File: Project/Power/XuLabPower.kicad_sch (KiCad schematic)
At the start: 16 parts, among them Q1 SQJ138ELP, Q2 SQJ138ELP, U1 LM74502

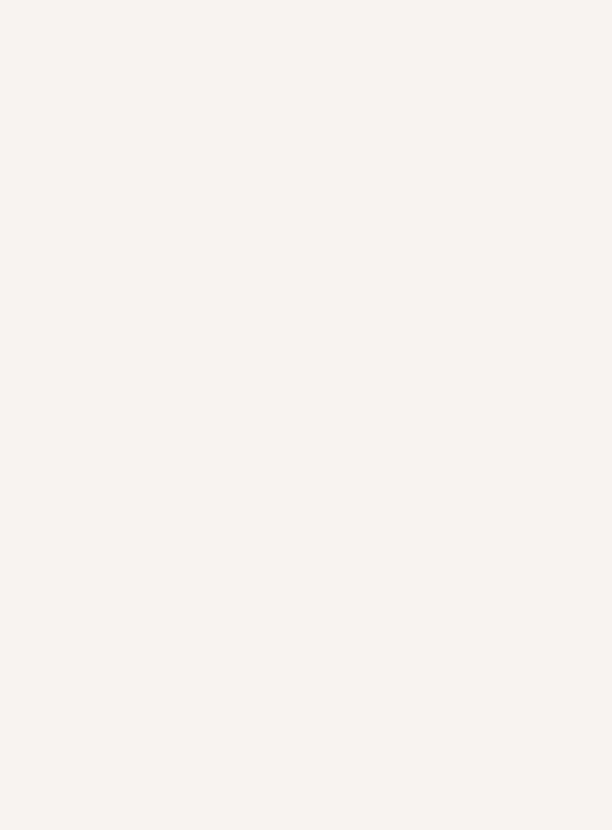
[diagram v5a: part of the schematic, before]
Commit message: Add STM32L422KBTx microcontroller
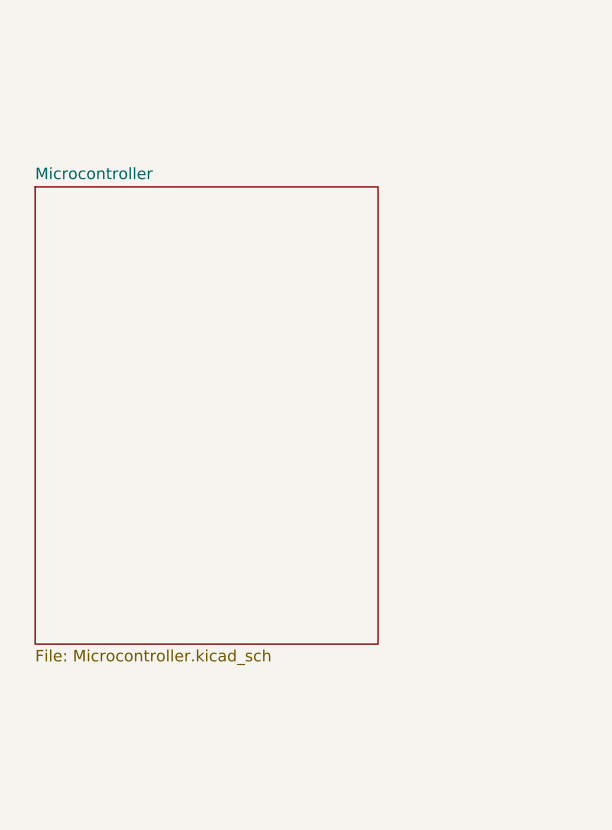
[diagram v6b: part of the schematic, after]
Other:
- added sheet Microcontroller (Microcontroller.kicad_sch)
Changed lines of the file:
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@@
+	)
+	(sheet
+		(at 38.1 88.9)
+		(size 38.1 50.8)
+		(exclude_from_sim no)
+		(in_bom yes)
+		(on_board yes)
+		(dnp no)
+		(fields_autoplaced yes)
+		(stroke
+			(width 0.1524)
+			(type solid)
+		)
+		(fill
+			(color 0 0 0 0.0000)
+		)
+		(property "Sheetname" "Microcontroller"
+			(at 38.1 88.1884 0)
+			(effects
+				(font
+					(size 1.27 1.27)
+				)
+				(justify left bottom)
+			)
+		)
+		(property "Sheetfile" "Microcontroller.kicad_sch"
+			(at 38.1 140.2846 0)
+			(effects
+				(font
+					(size 1.27 1.27)
+				)
+				(justify left top)
+			)
+		)
+		(instances
+			(project "XuLabPower"
+				(path "/71bb14ae-b730-4d22-a41d-cf68989dae2d"
+					(page "3")
+				)
+			)
+		)
 	)
 	(sheet
@@
 			(project "XuLabPower"
 				(path "/71bb14ae-b730-4d22-a41d-cf68989dae2d"
-					(page "3")
+					(page "4")
 				)
 			)

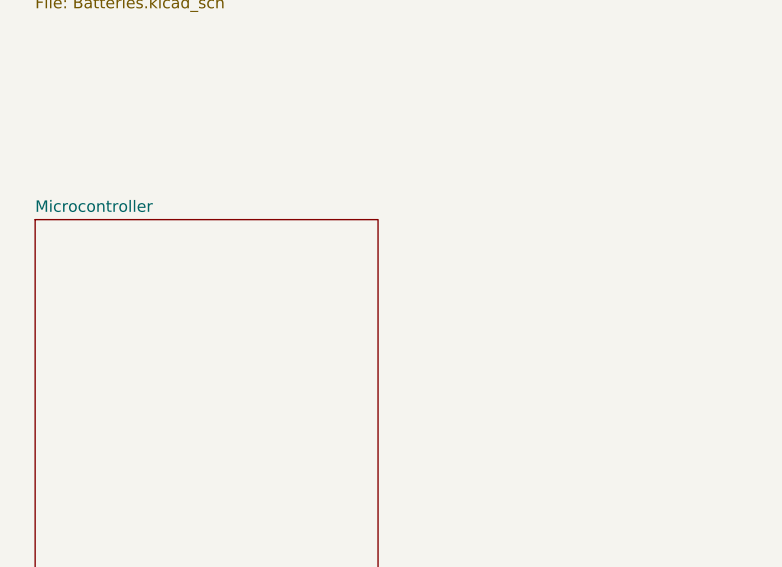
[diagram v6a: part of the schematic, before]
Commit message: Connect microcontroller to main enable switch
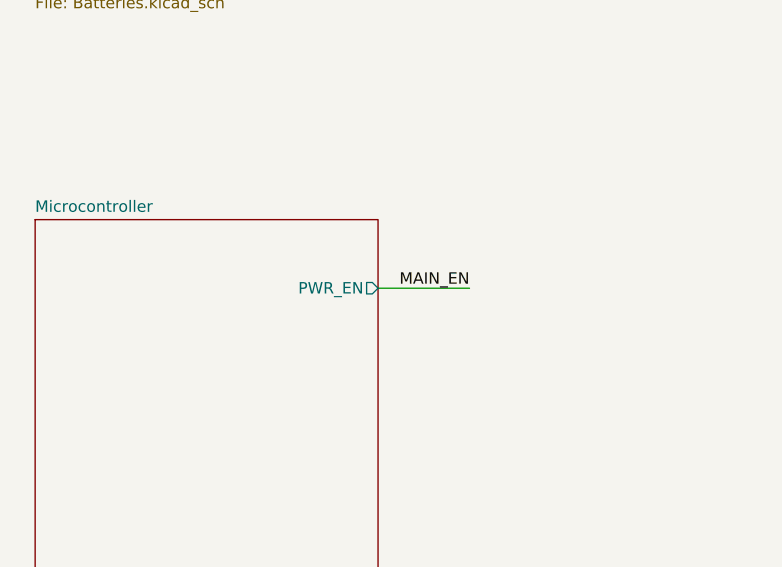
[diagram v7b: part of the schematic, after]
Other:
- sheet Microcontroller ports: added PWR_EN; removed none
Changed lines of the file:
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@@
 	(title_block
 		(title "Main Sheet")
-		(date "2026-03-08")
+		(date "2026-03-12")
 		(rev "B")
 		(company "CU Boulder Senior Design Team 29 - Xu Lab")
@@
 		(pts
 			(xy 222.25 46.99) (xy 223.52 46.99)
+		)
+		(stroke
+			(width 0)
+			(type default)
+		)
+	)
+	(wire
+		(pts
+			(xy 76.2 96.52) (xy 86.36 96.52)
 		)
 		(stroke
@@
 			)
 			(justify left bottom)
+		)
+	)
+	(label "MAIN_EN"
+		(at 86.36 96.52 180)
+		(effects
+			(font
+				(size 1.27 1.27)
+			)
+			(justify right bottom)
 		)
 	)
@@
 			)
 		)
+		(pin "PWR_EN" output
+			(at 76.2 96.52 0)
+			(effects
+				(font
+					(size 1.27 1.27)
+				)
+				(justify right)
+			)
+		)

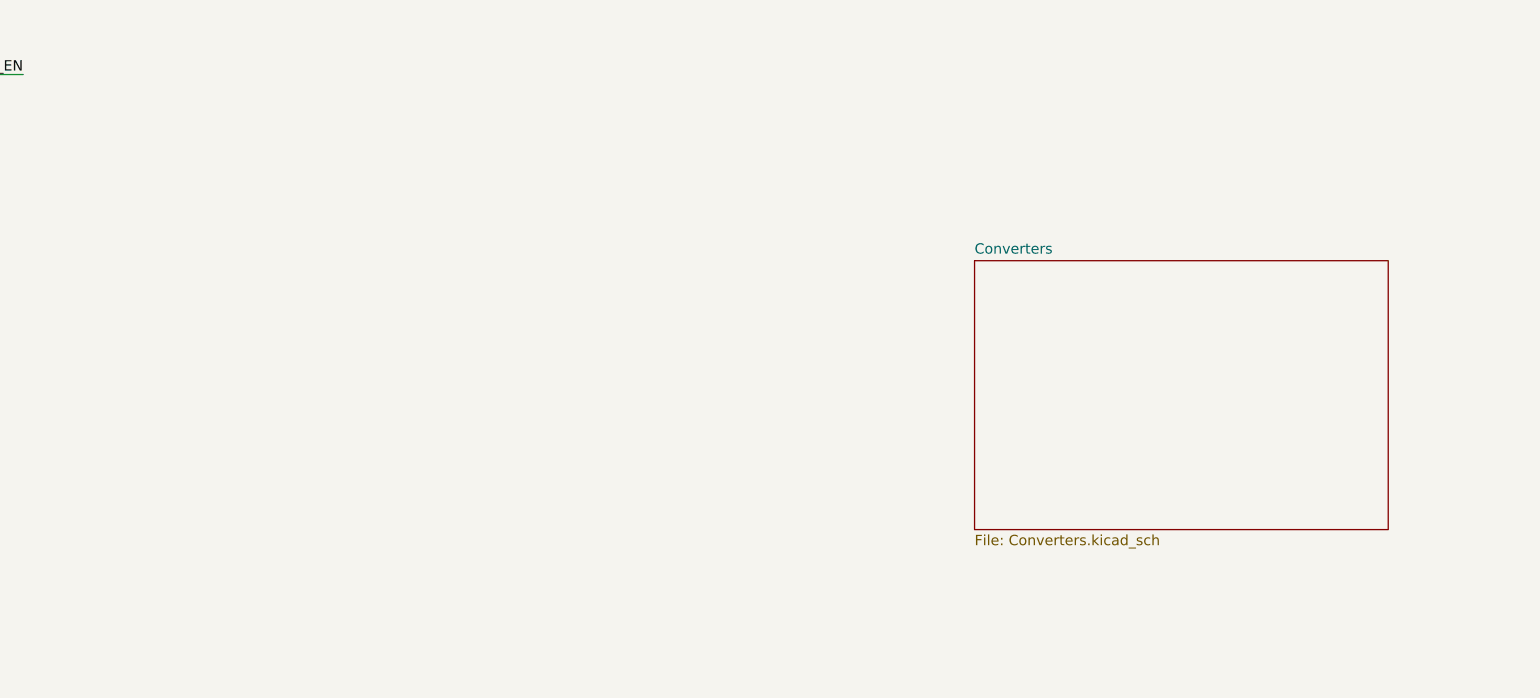
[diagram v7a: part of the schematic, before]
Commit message: Add servo connectors
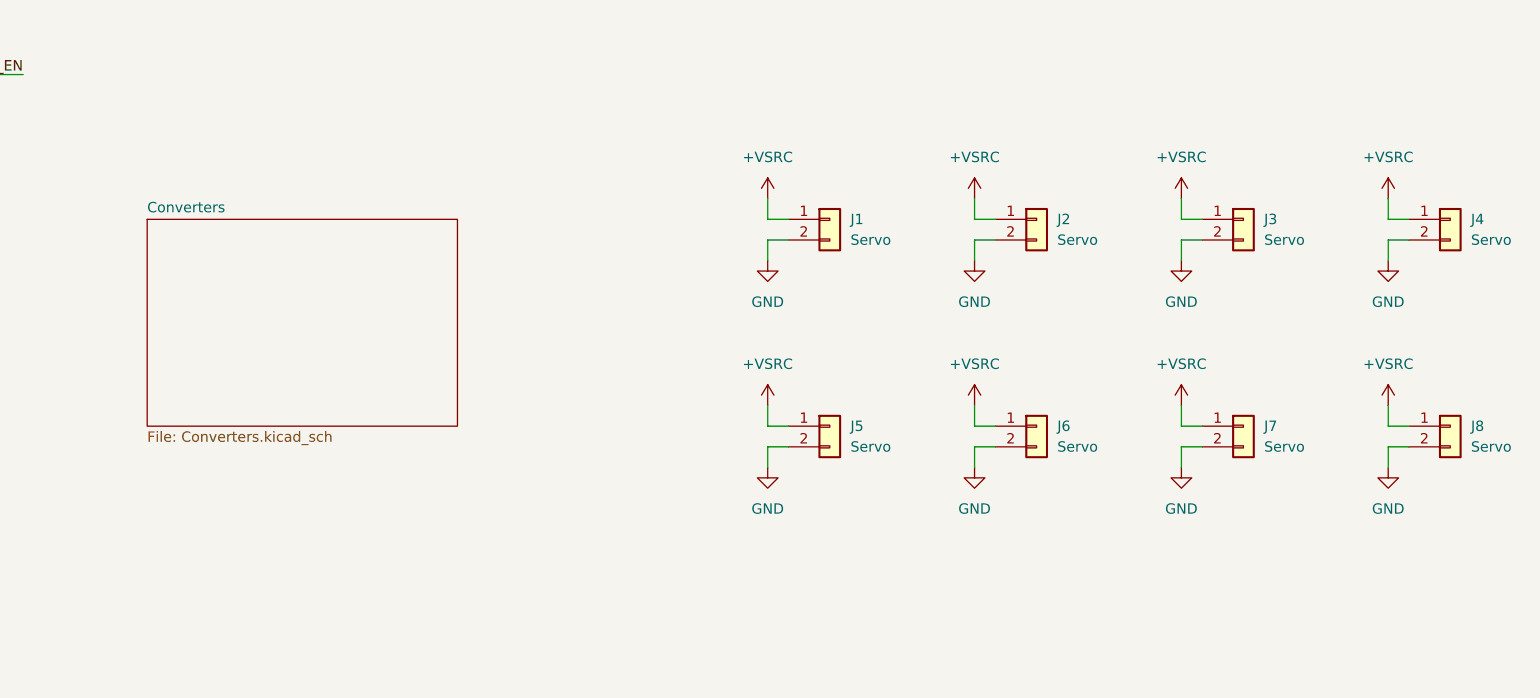
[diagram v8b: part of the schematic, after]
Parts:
- added J1, J2, J3, J4, J5, J6, J7, J8: Servo, Connector_JST:JST_VH_S2P-VH_1x02_P3.96mm_Horizontal, symbol Connector_Generic:Conn_01x02
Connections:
- net +VSRC: now also J1.1 (Pin_1), J2.1 (Pin_1), J3.1 (Pin_1), J4.1 (Pin_1), J5.1 (Pin_1), J6.1 (Pin_1), J7.1 (Pin_1), J8.1 (Pin_1)
- net GND: now also J1.2 (Pin_2), J2.2 (Pin_2), J3.2 (Pin_2), J4.2 (Pin_2), J5.2 (Pin_2), J6.2 (Pin_2), J7.2 (Pin_2), J8.2 (Pin_2)
